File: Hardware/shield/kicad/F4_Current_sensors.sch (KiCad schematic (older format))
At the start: 26 parts, among them U3 MCP6244

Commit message: move to digital 1.1.1
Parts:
- removed C12, C13, C14: 10uF, Capacitors_ThroughHole:C_Radial_D5_L6_P2.5, symbol C-RESCUE-Windlogger
- removed C15: 100nF, Capacitors_ThroughHole:C_Rect_L7_W2.5_P5, symbol C
- removed D12, D14, D15, D16, D17, D18: 1N4148, Discret:DO-35, symbol D
- removed R24, R28, R29, R30, R33, R34: 470k, Discret:R3-LARGE_PADS, symbol R-RESCUE-Windlogger
- removed R26, R31, R32: 680, Discret:R3-LARGE_PADS, symbol R-RESCUE-Windlogger
- removed U3: MCP6244, Housings_DIP:DIP-14_W7.62mm_LongPads, symbol MCP6004
- added C502, C503, C504: 10uF, Capacitors_ThroughHole:C_Radial_D5_L6_P2.5, symbol C-RESCUE-Windlogger
- added D503, D504, D505, D506, D507, D508: 1N4148, Diodes_ThroughHole:Diode_DO-35_SOD27_Horizontal_RM10, symbol D
- added JP501, JP502, JP503, JP504: JUMPER3, Pin_Headers:Pin_Header_Straight_1x03, symbol JUMPER3
- added R502, R509, R510: 180, Discret:R4, symbol R-RESCUE-Windlogger
- added R503, R504, R511, R512: 90.9, Discret:R4, symbol R-RESCUE-Windlogger
- added R507, R508, R513, R514, R515, R516: 100k, Discret:R4, symbol R-RESCUE-Windlogger
- added U401, U501, U502: LMV358, Housings_DIP:DIP-8_W7.62mm_LongPads, symbol LM358-RESCUE-Windlogger
- D501: renamed from D11; footprint Discret:DO-35 -> Diodes_ThroughHole:Diode_DO-35_SOD27_Horizontal_RM10
- D502: renamed from D13; footprint Discret:DO-35 -> Diodes_ThroughHole:Diode_DO-35_SOD27_Horizontal_RM10
- R501: renamed from R25; value 680 -> 180; footprint Discret:R3-LARGE_PADS -> Discret:R4
- R505: renamed from R23; value 470k -> 100k; footprint Discret:R3-LARGE_PADS -> Discret:R4
- R506: renamed from R27; value 470k -> 100k; footprint Discret:R3-LARGE_PADS -> Discret:R4
- renumbered C11 to C501
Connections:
- net +5V: now also D503.1 (K), D505.1 (K), D507.1 (K), R507.1, R513.1, R515.1, U401.8 (V+), U501.8 (V+), U501.8 (V+), U502.8 (V+)
- net GND: now also C502.2, C503.2, C504.2, D504.2 (A), D506.2 (A), D508.2 (A), R508.2, R514.2, R516.2, U401.4 (V-), U501.4 (V-), U501.4 (V-), U502.4 (V-)
- net I1: now also U401.6 (-), U401.7, U501.1, U501.2 (-), U501.6 (-), U501.7, U502.1, U502.2 (-)
- net I1_hi: now also JP501.2, U401.5 (+); no longer R501.1
- net I1_lo: now also R503.2
- net I2_hi: now also D503.2 (A), D504.1 (K), JP502.2, U501.3 (+)
- net I2_lo: now also C502.1, R502.2, R504.2, R507.2, R508.1
- net I3_hi: now also D507.2 (A), D508.1 (K), JP504.2, U502.3 (+)
- net I3_lo: now also C504.1, R510.2, R512.2, R515.2, R516.1
- net I4_hi: now also D505.2 (A), D506.1 (K), JP503.2, U501.5 (+)
- net I4_lo: now also C503.1, R509.2, R511.2, R513.2, R514.1
- new net 0-16A: JP501.3, JP502.3, JP503.3, JP504.3, R501.1, R502.1, R509.1, R510.1
- new net 0-32A: JP501.1, JP502.1, JP503.1, JP504.1, R503.1, R504.1, R511.1, R512.1
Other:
- note added: "Use the jumper to select the maximum current : 16 or 32 A\n"
- note removed: "Burden Resistor (ohms) = (AREF * CT TURNS) / (2√2 * max primary current)\n ex :\n180 : 16A\n90.9 : 32A\n"
- note removed: "Burden resistor"
- note removed: "Current sensor 1 , select the burden resistor value"
- note removed: "Current sensor 2 , select the burden resistor value"
- note removed: "Current sensor 3 , select the burden resistor value"
- note removed: "Current sensor 4 , select the burden resistor value"
- note removed: "No sold burden resistor\nfor DC current"
- moved on the sheet: C501, D501, D502, R501, R505, R506

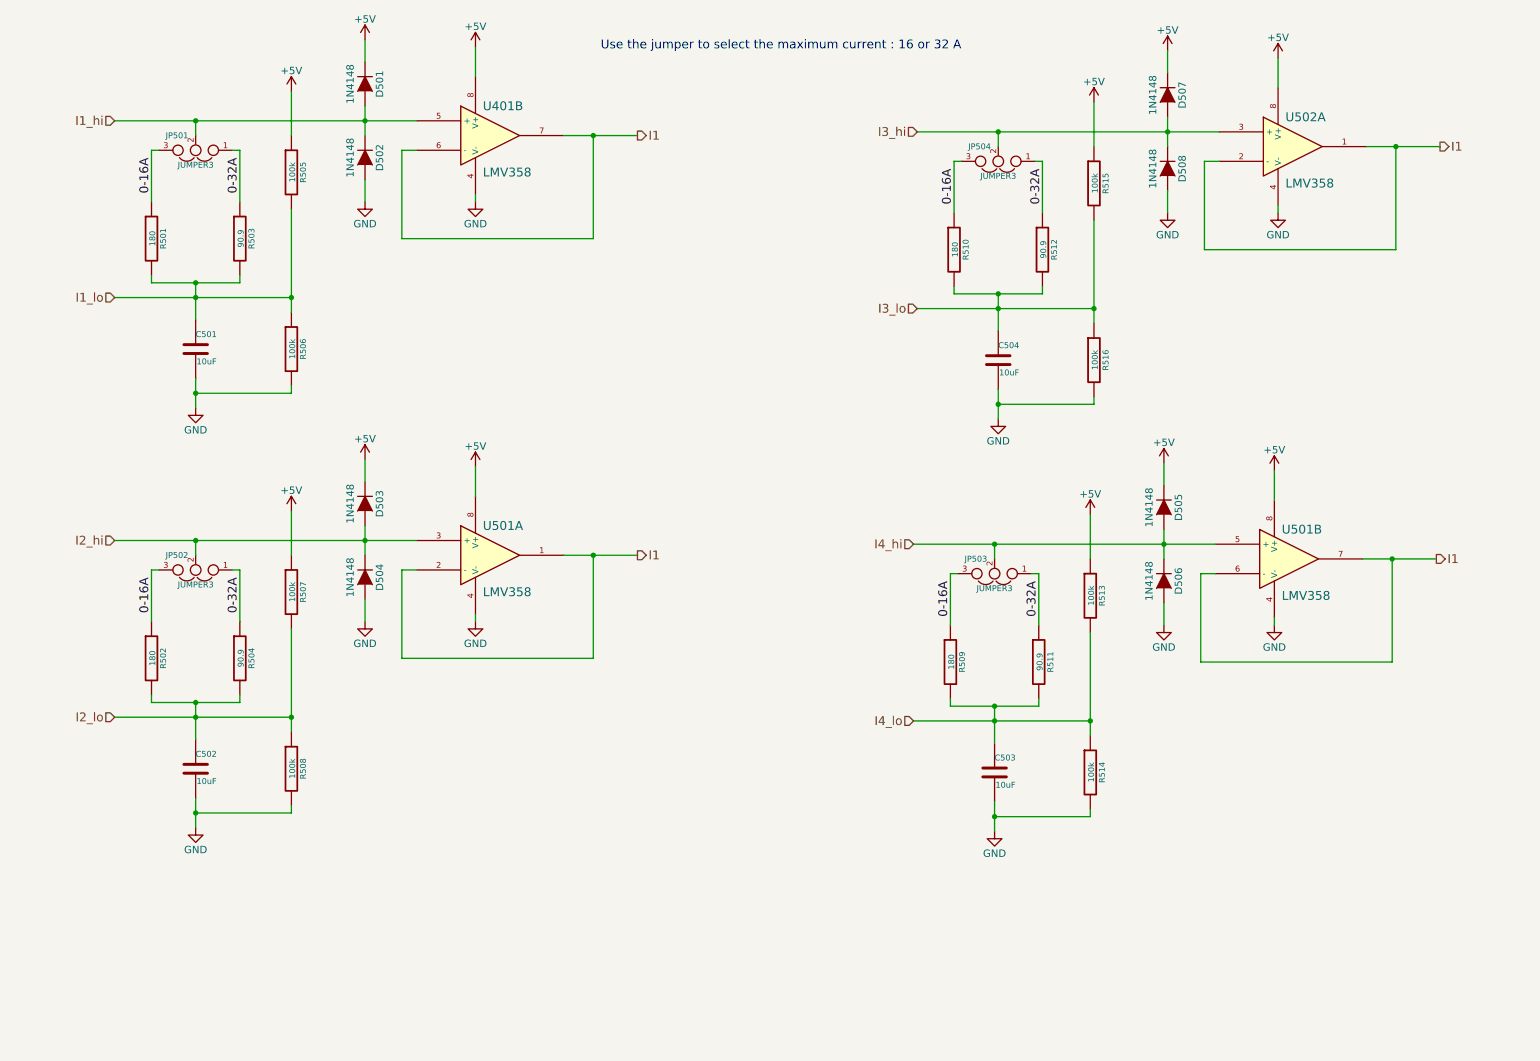
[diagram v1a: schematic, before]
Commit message: Update shield to 2.0.0
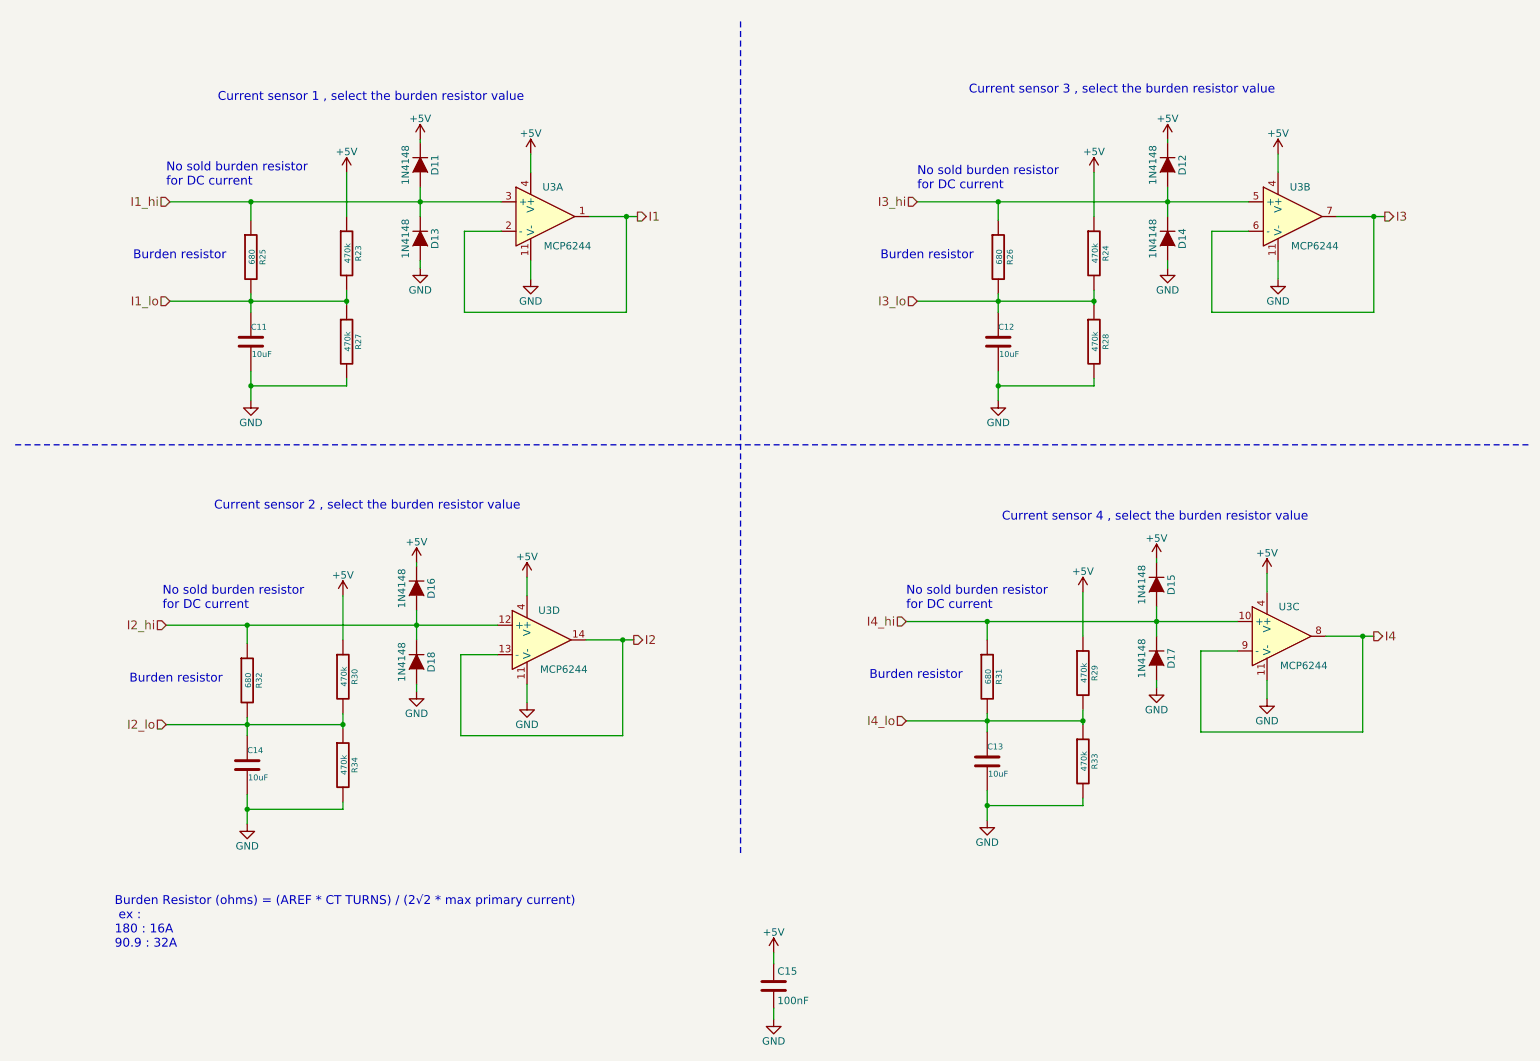
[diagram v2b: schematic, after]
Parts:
- removed C502, C503, C504: 10uF, Capacitors_ThroughHole:C_Radial_D5_L6_P2.5, symbol C-RESCUE-Windlogger
- removed D503, D504, D505, D506, D507, D508: 1N4148, Diodes_ThroughHole:Diode_DO-35_SOD27_Horizontal_RM10, symbol D
- removed JP501, JP502, JP503, JP504: JUMPER3, Pin_Headers:Pin_Header_Straight_1x03, symbol JUMPER3
- removed R502, R509, R510: 180, Discret:R4, symbol R-RESCUE-Windlogger
- removed R503, R504, R511, R512: 90.9, Discret:R4, symbol R-RESCUE-Windlogger
- removed R507, R508, R513, R514, R515, R516: 100k, Discret:R4, symbol R-RESCUE-Windlogger
- removed U401, U501, U502: LMV358, Housings_DIP:DIP-8_W7.62mm_LongPads, symbol LM358-RESCUE-Windlogger
- added C12, C13, C14: 10uF, Capacitors_ThroughHole:C_Radial_D5_L6_P2.5, symbol C-RESCUE-Windlogger
- added C15: 100nF, Capacitors_ThroughHole:C_Rect_L7_W2.5_P5, symbol C
- added D12, D14, D15, D16, D17, D18: 1N4148, Discret:DO-35, symbol D
- added R24, R28, R29, R30, R33, R34: 470k, Discret:R3-LARGE_PADS, symbol R-RESCUE-Windlogger
- added R26, R31, R32: 680, Discret:R3-LARGE_PADS, symbol R-RESCUE-Windlogger
- added U3: MCP6244, Housings_DIP:DIP-14_W7.62mm_LongPads, symbol MCP6004
- D11: renamed from D501; footprint Diodes_ThroughHole:Diode_DO-35_SOD27_Horizontal_RM10 -> Discret:DO-35
- D13: renamed from D502; footprint Diodes_ThroughHole:Diode_DO-35_SOD27_Horizontal_RM10 -> Discret:DO-35
- R23: renamed from R505; value 100k -> 470k; footprint Discret:R4 -> Discret:R3-LARGE_PADS
- R25: renamed from R501; value 180 -> 680; footprint Discret:R4 -> Discret:R3-LARGE_PADS
- R27: renamed from R506; value 100k -> 470k; footprint Discret:R4 -> Discret:R3-LARGE_PADS
- renumbered C501 to C11
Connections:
- net 0-16A is gone; now on net I1_hi: R25.1
- net +5V: now also C15.1, D12.1 (K), D15.1 (K), D16.1 (K), R24.1, R29.1, R30.1, U3.4 (V+), U3.4 (V+), U3.4 (V+), U3.4 (V+)
- net GND: now also C12.2, C13.2, C14.2, C15.2, D14.2 (A), D17.2 (A), D18.2 (A), R28.2, R33.2, R34.2, U3.11 (V-), U3.11 (V-), U3.11 (V-), U3.11 (V-)
- net I1: now also U3.1, U3.2 (-)
- net I1_hi: now also U3.3 (+)
- net I2_hi: now also D16.2 (A), D18.1 (K), R32.1, U3.12 (+)
- net I2_lo: now also C14.1, R30.2, R32.2, R34.1
- net I3_hi: now also D12.2 (A), D14.1 (K), R26.1, U3.5 (+)
- net I3_lo: now also C12.1, R24.2, R26.2, R28.1
- net I4_hi: now also D15.2 (A), D17.1 (K), R31.1, U3.10 (+)
- net I4_lo: now also C13.1, R29.2, R31.2, R33.1
- new net I2: U3.13 (-), U3.14
- new net I3: U3.6 (-), U3.7
- new net I4: U3.8, U3.9 (-)
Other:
- note added: "Burden Resistor (ohms) = (AREF * CT TURNS) / (2√2 * max primary current)\n ex :\n180 : 16A\n90.9 : 32A\n"
- note added: "Burden resistor"
- note added: "Current sensor 1 , select the burden resistor value"
- note added: "Current sensor 2 , select the burden resistor value"
- note added: "Current sensor 3 , select the burden resistor value"
- note added: "Current sensor 4 , select the burden resistor value"
- note added: "No sold burden resistor\nfor DC current"
- note removed: "Use the jumper to select the maximum current : 16 or 32 A\n"
- moved on the sheet: C11, D11, D13, R23, R25, R27
